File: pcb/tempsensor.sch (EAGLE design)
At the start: 18 parts, among them Q1 DS18X20TO92, Q2 DS18X20SO-8

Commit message: Update PCB
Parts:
- renumbered U$3 to U1
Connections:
- net RX_5V: now also R1.1, T1.S; no longer R5.2
- net TX: now also R3.1, T1.D; no longer R1.1, T1.S
- net TX_5V: now also R5.2; no longer R3.1, T1.D
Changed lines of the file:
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@@
 <part name="P+8" library="supply1" deviceset="VCC" device=""/>
 <part name="GND6" library="supply1" deviceset="GND" device=""/>
-<part name="U$3" library="esp8266modules" deviceset="ESP8266" device=""/>
+<part name="U1" library="esp8266modules" deviceset="ESP8266" device=""/>
 <part name="P+9" library="supply1" deviceset="VCC" device=""/>
 <part name="GND7" library="supply1" deviceset="GND" device=""/>
@@
 <instance part="P+8" gate="VCC" x="93.98" y="10.16" rot="R270"/>
 <instance part="GND6" gate="1" x="76.2" y="10.16" rot="R270"/>
-<instance part="U$3" gate="G$1" x="53.34" y="88.9"/>
+<instance part="U1" gate="G$1" x="53.34" y="88.9"/>
 <instance part="P+9" gate="VCC" x="35.56" y="99.06"/>
 <instance part="GND7" gate="1" x="71.12" y="81.28" rot="R90"/>
@@
 </segment>
 <segment>
-<pinref part="U$3" gate="G$1" pin="VCC"/>
+<pinref part="U1" gate="G$1" pin="VCC"/>
 <pinref part="P+9" gate="VCC" pin="VCC"/>
 </segment>
@@
 </segment>
 <segment>
-<pinref part="U$3" gate="G$1" pin="CH_PD"/>
+<pinref part="U1" gate="G$1" pin="CH_PD"/>
 <pinref part="P+1" gate="VCC" pin="VCC"/>
 <wire x1="73.66" y1="93.98" x2="68.58" y2="93.98" width="0.1524" layer="91"/>
@@
 </segment>
 <segment>
-<pinref part="U$3" gate="G$1" pin="GND"/>
+<pinref part="U1" gate="G$1" pin="GND"/>
 <pinref part="GND7" gate="1" pin="GND"/>
 </segment>
 <segment>
-<pinref part="U$3" gate="G$1" pin="GPIO15"/>
+<pinref part="U1" gate="G$1" pin="GPIO15"/>
 <pinref part="GND8" gate="1" pin="GND"/>
 </segment>
@@
 <wire x1="68.58" y1="88.9" x2="76.2" y2="88.9" width="0.1524" layer="91"/>
 <label x="73.66" y="88.9" size="1.778" layer="95"/>
-<pinref part="U$3" gate="G$1" pin="URXD"/>
-<junction x="68.58" y="88.9"/>
+<pinref part="U1" gate="G$1" pin="URXD"/>
 </segment>
 <segment>
@@
 <wire x1="68.58" y1="86.36" x2="76.2" y2="86.36" width="0.1524" layer="91"/>
 <label x="73.66" y="86.36" size="1.778" layer="95"/>
-<pinref part="U$3" gate="G$1" pin="UTXD"/>
-<junction x="68.58" y="86.36"/>
-</segment>
-<segment>
-<pinref part="T1" gate="A" pin="S"/>
-<pinref part="R1" gate="G$1" pin="1"/>
-<wire x1="15.24" y1="45.72" x2="12.7" y2="45.72" width="0.1524" layer="91"/>
-<wire x1="12.7" y1="45.72" x2="5.08" y2="45.72" width="0.1524" layer="91"/>
-<junction x="12.7" y="45.72"/>
-<label x="5.08" y="45.72" size="1.778" layer="95"/>
+<pinref part="U1" gate="G$1" pin="UTXD"/>
+</segment>
+<segment>
+<pinref part="T1" gate="A" pin="D"/>
+<pinref part="R3" gate="G$1" pin="1"/>
+<wire x1="25.4" y1="45.72" x2="27.94" y2="45.72" width="0.1524" layer="91"/>
+<wire x1="27.94" y1="45.72" x2="33.02" y2="45.72" width="0.1524" layer="91"/>
+<junction x="27.94" y="45.72"/>
+<label x="33.02" y="45.72" size="1.778" layer="95"/>
 </segment>
 </net>
@@
 </segment>
 <segment>
-<pinref part="U$3" gate="G$1" pin="GPIO2"/>
+<pinref part="U1" gate="G$1" pin="GPIO2"/>
 <pinref part="R4" gate="G$1" pin="2"/>
 <wire x1="35.56" y1="83.82" x2="25.4" y2="83.82" width="0.1524" layer="91"/>
@@
 <net name="N$1" class="0">
 <segment>
-<pinref part="U$3" gate="G$1" pin="GPIO0"/>
+<pinref part="U1" gate="G$1" pin="GPIO0"/>
 <pinref part="R2" gate="G$1" pin="2"/>
 <wire x1="35.56" y1="81.28" x2="35.56" y2="78.74" width="0.1524" layer="91"/>
@@
 <net name="N$2" class="0">
 <segment>
-<pinref part="U$3" gate="G$1" pin="GPIO13"/>
+<pinref part="U1" gate="G$1" pin="GPIO13"/>
 <pinref part="TP3" gate="G$1" pin="TP"/>
 <wire x1="35.56" y1="88.9" x2="20.32" y2="88.9" width="0.1524" layer="91"/>
@@
 <segment>
 <pinref part="TP2" gate="G$1" pin="TP"/>
-<pinref part="U$3" gate="G$1" pin="GPIO12"/>
+<pinref part="U1" gate="G$1" pin="GPIO12"/>
 <wire x1="25.4" y1="91.44" x2="35.56" y2="91.44" width="0.1524" layer="91"/>
 </segment>
@@
 <net name="N$4" class="0">
 <segment>
-<pinref part="U$3" gate="G$1" pin="GPIO14"/>
+<pinref part="U1" gate="G$1" pin="GPIO14"/>
 <pinref part="TP1" gate="G$1" pin="TP"/>
 <wire x1="35.56" y1="93.98" x2="30.48" y2="93.98" width="0.1524" layer="91"/>
@@
 </segment>
 <segment>
-<pinref part="T1" gate="A" pin="D"/>
-<pinref part="R3" gate="G$1" pin="1"/>
-<wire x1="25.4" y1="45.72" x2="27.94" y2="45.72" width="0.1524" layer="91"/>
-<wire x1="27.94" y1="45.72" x2="33.02" y2="45.72" width="0.1524" layer="91"/>
-<junction x="27.94" y="45.72"/>
-<label x="33.02" y="45.72" size="1.778" layer="95"/>
+<pinref part="R5" gate="G$1" pin="2"/>
+<wire x1="-20.32" y1="38.1" x2="-12.7" y2="38.1" width="0.1524" layer="91"/>
+<label x="-17.78" y="38.1" size="1.778" layer="95"/>
 </segment>
 </net>
@@
 </segment>
 <segment>
-<pinref part="R5" gate="G$1" pin="2"/>
-<wire x1="-20.32" y1="38.1" x2="-12.7" y2="38.1" width="0.1524" layer="91"/>
-<label x="-17.78" y="38.1" size="1.778" layer="95"/>
-</segment>
-</net>
+<pinref part="T1" gate="A" pin="S"/>
+<pinref part="R1" gate="G$1" pin="1"/>
+<wire x1="15.24" y1="45.72" x2="12.7" y2="45.72" width="0.1524" layer="91"/>
+<wire x1="12.7" y1="45.72" x2="0" y2="45.72" width="0.1524" layer="91"/>
+<junction x="12.7" y="45.72"/>
+<label x="0" y="45.72" size="1.778" layer="95"/>
+</segment>
+</net>

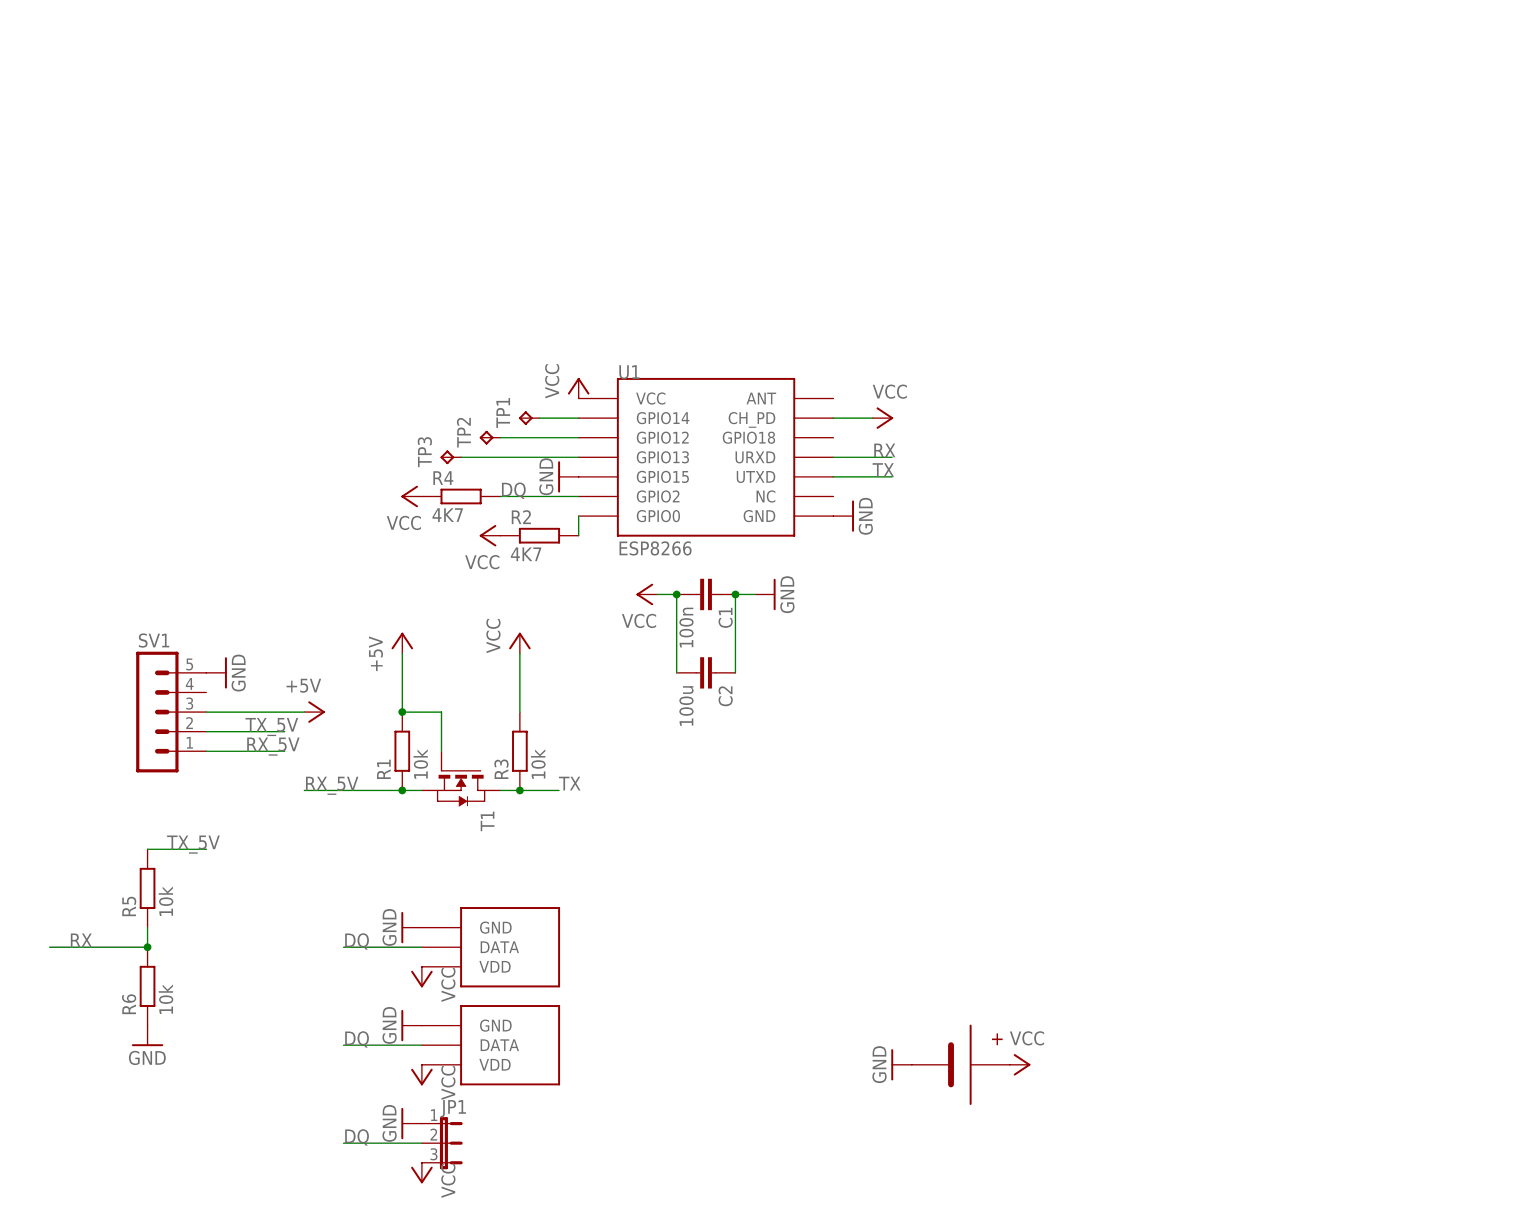
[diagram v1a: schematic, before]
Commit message: Update PCB: Add lipo charging circuit based on mcp73831 and Reset und Program buttons
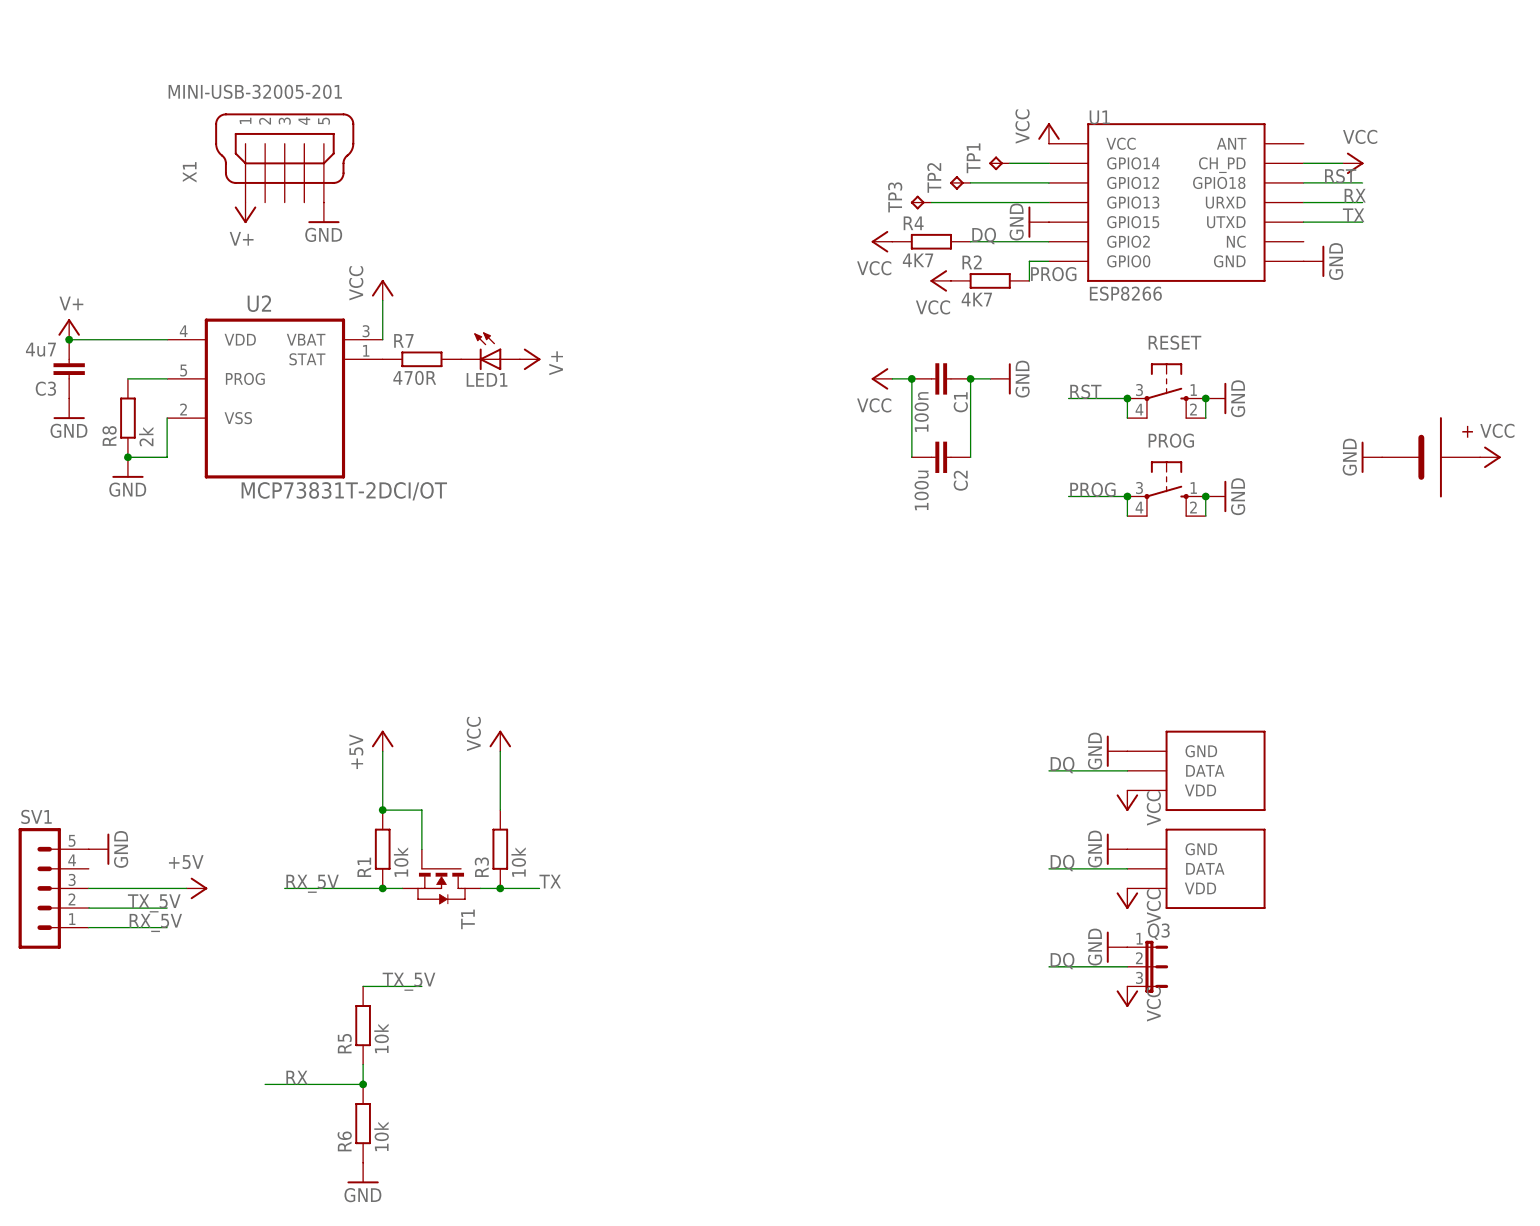
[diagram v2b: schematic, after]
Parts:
- removed JP1: (no value), jumper:JP2E
- added C3: 4u7, resistor:C-EUC0805
- added LED1: (no value), led:LEDCHIPLED_0805
- added PROG, RESET: (no value), switch-omron:10-XX
- added Q3: (no value), jumper:JP2E
- added R7: 470R, resistor:R-EU_M0805
- added R8: 2k, resistor:R-EU_M0805
- added U2: MCP73831T-2DCI/OT, Microchip-MCP73831T-2DCI_OT:MCP73831T-2DCI/OT
- added X1: MINI-USB-32005-201, con-cypressindustries:MINI-USB-32005-201
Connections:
- new net N$5: LED1.C, R7.2
- new net N$6: R8.2, U2.PROG
- new net PROG: PROG.P, PROG.P1, R2.2, U1.GPIO0
- new net RST: RESET.P, RESET.P1, U1.GPIO18
- new net V+: C3.2, LED1.A, U2.VDD, X1.1
- net DQ: now also Q3.2; no longer JP1.2
- net GND: now also C3.1, PROG.S, PROG.S1, Q3.1, R8.1, RESET.S, RESET.S1, U2.VSS, X1.5; no longer JP1.1
- net N$1: now also R7.1, U2.STAT; no longer R2.2, U1.GPIO0
- net VCC: now also Q3.3, U2.VBAT; no longer JP1.3
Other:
- moved on the sheet: C1, C2, R1, R2, R3, R4, R5, R6, SV1, T1, TP1, TP2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

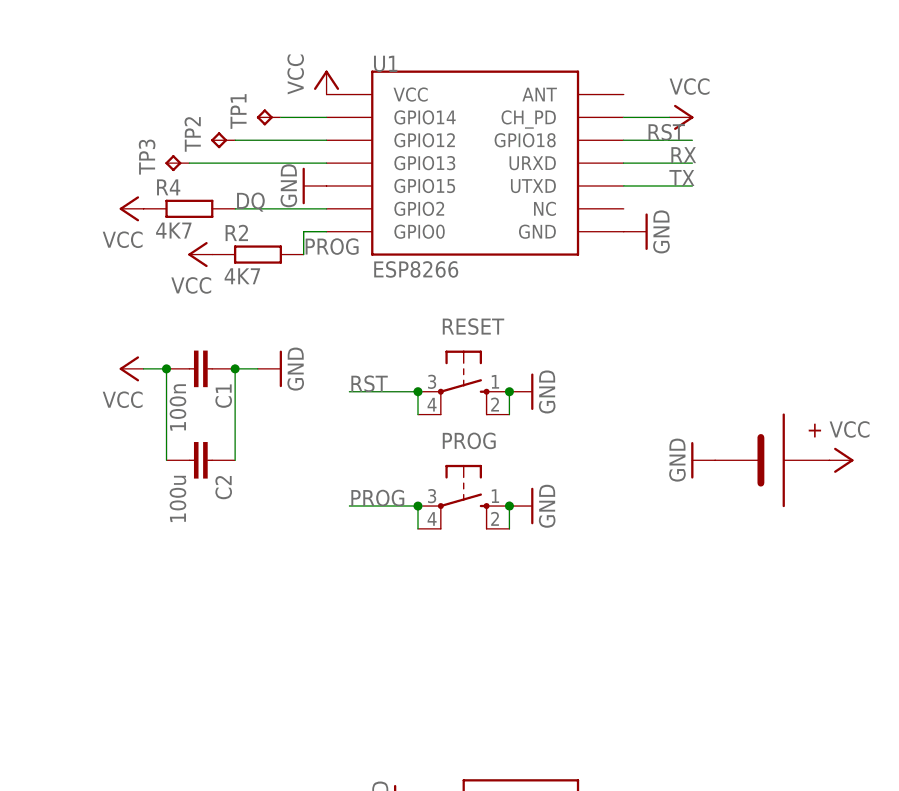
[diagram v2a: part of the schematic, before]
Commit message: PCB: add optional pullup resistor for RESET pin, and additional 100u cap for power
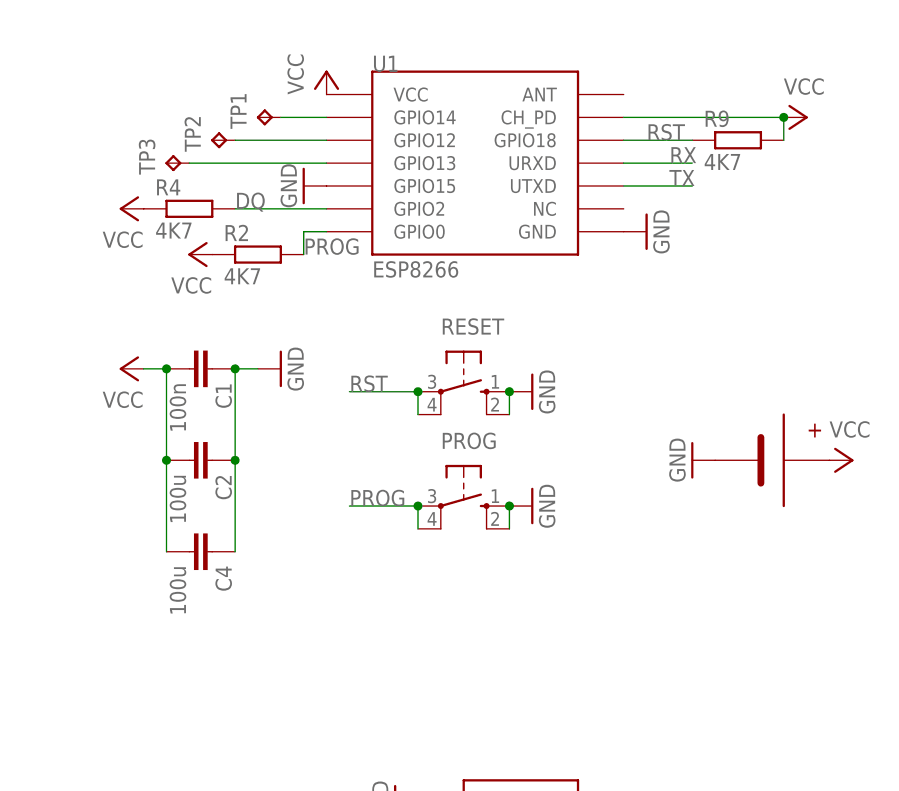
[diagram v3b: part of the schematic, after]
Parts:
- added C4: 100u, resistor:C-EUC1206
- added R9: 4K7, resistor:R-EU_M0805
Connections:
- net GND: now also C4.1
- net RST: now also R9.1
- net VCC: now also C4.2, R9.2
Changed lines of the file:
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@@
 <part name="GND14" library="supply1" deviceset="GND" device=""/>
 <part name="SUPPLY3" library="supply2" deviceset="V+" device=""/>
+<part name="R9" library="resistor" deviceset="R-EU_" device="M0805" value="4K7"/>
+<part name="C4" library="resistor" deviceset="C-EU" device="C1206" value="100u"/>
 </parts>
 <sheets>
@@
 <instance part="R4" gate="G$1" x="81.28" y="116.84"/>
 <instance part="P+10" gate="VCC" x="73.66" y="116.84" rot="R90"/>
-<instance part="P+1" gate="VCC" x="137.16" y="127" rot="R270"/>
+<instance part="P+1" gate="VCC" x="149.86" y="127" rot="R270"/>
 <instance part="FRAME1" gate="G$1" x="-83.82" y="-27.94"/>
 <instance part="TP1" gate="G$1" x="88.9" y="127" rot="R90"/>
@@
 <instance part="GND14" gate="1" x="2.54" y="119.38"/>
 <instance part="SUPPLY3" gate="1" x="-7.62" y="119.38" rot="R180"/>
+<instance part="R9" gate="G$1" x="142.24" y="124.46"/>
+<instance part="C4" gate="G$1" x="83.82" y="78.74" rot="R270"/>
 </instances>
 <busses>
@@
 <wire x1="78.74" y1="88.9" x2="78.74" y2="99.06" width="0.1524" layer="91"/>
 <junction x="78.74" y="99.06"/>
+<pinref part="C4" gate="G$1" pin="2"/>
+<wire x1="78.74" y1="78.74" x2="78.74" y2="88.9" width="0.1524" layer="91"/>
+<junction x="78.74" y="88.9"/>
 </segment>
 <segment>
@@
 <pinref part="U1" gate="G$1" pin="CH_PD"/>
 <pinref part="P+1" gate="VCC" pin="VCC"/>
-<wire x1="134.62" y1="127" x2="129.54" y2="127" width="0.1524" layer="91"/>
+<wire x1="147.32" y1="127" x2="129.54" y2="127" width="0.1524" layer="91"/>
+<pinref part="R9" gate="G$1" pin="2"/>
+<wire x1="147.32" y1="124.46" x2="147.32" y2="127" width="0.1524" layer="91"/>
+<junction x="147.32" y="127"/>
 </segment>
 <segment>
@@
 <wire x1="86.36" y1="88.9" x2="86.36" y2="99.06" width="0.1524" layer="91"/>
 <junction x="86.36" y="99.06"/>
+<pinref part="C4" gate="G$1" pin="1"/>
+<wire x1="86.36" y1="78.74" x2="86.36" y2="88.9" width="0.1524" layer="91"/>
+<junction x="86.36" y="88.9"/>
 </segment>
 <segment>
@@
 <wire x1="129.54" y1="124.46" x2="137.16" y2="124.46" width="0.1524" layer="91"/>
 <label x="132.08" y="124.46" size="1.778" layer="95"/>
-</segment>
-<segment>
+<pinref part="R9" gate="G$1" pin="1"/>
+</segment>
+<segment>
